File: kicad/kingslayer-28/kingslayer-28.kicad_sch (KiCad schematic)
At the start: 77 parts, among them IC1 STM32F303CCT7, IC3 LM3940IMP-3.3_NOPB, J1 Conn_01x04_Pin, K1 KEYSW, K10 KEYSW, K11 KEYSW, K12 KEYSW, K13 KEYSW, K14 KEYSW, K15 KEYSW, K16 KEYSW, K17 KEYSW, K18 KEYSW, K19 KEYSW, K2 KEYSW, K20 KEYSW, K21 KEYSW, K22 KEYSW, K23 KEYSW, K24 KEYSW, K25 KEYSW, K26 KEYSW, K27 KEYSW, K28 KEYSW, K3 KEYSW, K4 KEYSW, K5 KEYSW, K6 KEYSW, K7 KEYSW, K8 KEYSW, K9 KEYSW, SW1 MSS13PLP, X1 IC21008.000M30.0EE1B

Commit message: assign some footprints
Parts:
- D1, D10, D11, D12, D13, D14, D15, D16, D17, D18, D19, D2, D20, D21, D22, D23, D24, D25, D26, D27, D28, D3, D4, D5, D6, D7, D8, D9: footprint (none) -> 1N4148W_RHG:1N4148WRHG
- IC1: footprint QFP50P900X900X160-48N -> STM32F303CCT7:QFP50P900X900X160-48N
- IC3: footprint SOT230P700X180-4N -> LM3940IMP-3.3_NOPB:SOT230P700X180-4N
- K1, K10, K11, K12, K13, K14, K15, K16, K17, K18, K19, K2, K20, K21, K22, K23, K24, K25, K26, K27, K28, K3, K4, K5, K6, K7, K8, K9: footprint (none) -> keyswitches:Kailh_socket_MX
- S1: footprint TL3342F260QG -> TL3342F260QG:TL3342F260QG
- USB1: footprint (none) -> Type-C:USB_C_GCT_USB4085

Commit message: update mounting holes
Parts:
- added H1: MountingHole, keyswitches:Stabilizer_MX_2u, symbol Mechanical:MountingHole
- added H2, H3, H4, H5: MountingHole, MountingHole:MountingHole_2.2mm_M2_ISO7380, symbol Mechanical:MountingHole
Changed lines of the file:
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@@
+    )
+  )
+  (symbol (lib_id "Mechanical:MountingHole") (at 193.04 102.87 0) (unit 1)
+    (in_bom yes) (on_board yes) (dnp no) (fields_autoplaced)
+    (property "Reference" "H2" (at 195.58 101.6 0)
+      (effects (font (size 1.27 1.27)) (justify left))
+    )
+    (property "Value" "MountingHole" (at 195.58 104.14 0)
+      (effects (font (size 1.27 1.27)) (justify left))
+    )
+    (property "Footprint" "MountingHole:MountingHole_2.2mm_M2_ISO7380" (at 193.04 102.87 0)
+      (effects (font (size 1.27 1.27)) hide)
+    )
+    (property "Datasheet" "~" (at 193.04 102.87 0)
+      (effects (font (size 1.27 1.27)) hide)
+    )
+    (instances
+      (project "kingslayer-28"
+        (path "/7c3679ab-fb1a-4578-bd30-c0b9ef7b8f3d"
+          (reference "H2") (unit 1)
+        )
+      )
     )
   )
@@
     )
   )
+  (symbol (lib_id "Mechanical:MountingHole") (at 215.9 114.3 0) (unit 1)
+    (in_bom yes) (on_board yes) (dnp no) (fields_autoplaced)
+    (property "Reference" "H5" (at 218.44 113.03 0)
+      (effects (font (size 1.27 1.27)) (justify left))
+    )
+    (property "Value" "MountingHole" (at 218.44 115.57 0)
+      (effects (font (size 1.27 1.27)) (justify left))
+    )
+    (property "Footprint" "MountingHole:MountingHole_2.2mm_M2_ISO7380" (at 215.9 114.3 0)
+      (effects (font (size 1.27 1.27)) hide)
+    )
+    (property "Datasheet" "~" (at 215.9 114.3 0)
+      (effects (font (size 1.27 1.27)) hide)
+    )
+    (instances
+      (project "kingslayer-28"
+        (path "/7c3679ab-fb1a-4578-bd30-c0b9ef7b8f3d"
+          (reference "H5") (unit 1)
+        )
+      )
+    )
+  )
   (symbol (lib_id "keyboard_parts:+3V3") (at 237.49 38.1 0) (unit 1)
     (in_bom yes) (on_board yes) (dnp no) (fields_autoplaced)
@@
     )
   )
+  (symbol (lib_id "Mechanical:MountingHole") (at 137.16 81.28 0) (unit 1)
+    (in_bom yes) (on_board yes) (dnp no) (fields_autoplaced)
+    (property "Reference" "H1" (at 139.7 80.01 0)
+      (effects (font (size 1.27 1.27)) (justify left))
+    )
+    (property "Value" "MountingHole" (at 139.7 82.55 0)
+      (effects (font (size 1.27 1.27)) (justify left))
+    )
+    (property "Footprint" "keyswitches:Stabilizer_MX_2u" (at 137.16 81.28 0)
+      (effects (font (size 1.27 1.27)) hide)
+    )
+    (property "Datasheet" "~" (at 137.16 81.28 0)
+      (effects (font (size 1.27 1.27)) hide)
+    )
+    (instances
+      (project "kingslayer-28"
+        (path "/7c3679ab-fb1a-4578-bd30-c0b9ef7b8f3d"
+          (reference "H1") (unit 1)
+        )
+      )
+    )
+  )
   (symbol (lib_id "keyboard_parts:KEYSW") (at 71.12 39.37 0) (unit 1)
     (in_bom yes) (on_board yes) (dnp no)
@@
     )
   )
+  (symbol (lib_id "Mechanical:MountingHole") (at 193.04 114.3 0) (unit 1)
+    (in_bom yes) (on_board yes) (dnp no) (fields_autoplaced)
+    (property "Reference" "H4" (at 195.58 113.03 0)
+      (effects (font (size 1.27 1.27)) (justify left))
+    )
+    (property "Value" "MountingHole" (at 195.58 115.57 0)
+      (effects (font (size 1.27 1.27)) (justify left))
+    )
+    (property "Footprint" "MountingHole:MountingHole_2.2mm_M2_ISO7380" (at 193.04 114.3 0)
+      (effects (font (size 1.27 1.27)) hide)
+    )
+    (property "Datasheet" "~" (at 193.04 114.3 0)
+      (effects (font (size 1.27 1.27)) hide)
+    )
+    (instances
+      (project "kingslayer-28"
+        (path "/7c3679ab-fb1a-4578-bd30-c0b9ef7b8f3d"
+          (reference "H4") (unit 1)
+        )
+      )
+    )
+  )
   (symbol (lib_id "keyboard_parts:D") (at 63.5 82.55 180) (unit 1)
     (in_bom yes) (on_board yes) (dnp no) (fields_autoplaced)
@@
         )
       )
+    )
+  )
+  (symbol (lib_id "Mechanical:MountingHole") (at 215.9 102.87 0) (unit 1)
+    (in_bom yes) (on_board yes) (dnp no) (fields_autoplaced)
+    (property "Reference" "H3" (at 218.44 101.6 0)
+      (effects (font (size 1.27 1.27)) (justify left))
+    )
+    (property "Value" "MountingHole" (at 218.44 104.14 0)
+      (effects (font (size 1.27 1.27)) (justify left))
+    )
+    (property "Footprint" "MountingHole:MountingHole_2.2mm_M2_ISO7380" (at 215.9 102.87 0)
+      (effects (font (size 1.27 1.27)) hide)
+    )
+    (property "Datasheet" "~" (at 215.9 102.87 0)
+      (effects (font (size 1.27 1.27)) hide)
+    )
+    (instances
+      (project "kingslayer-28"
+        (path "/7c3679ab-fb1a-4578-bd30-c0b9ef7b8f3d"
+          (reference "H3") (unit 1)
+        )
+      )

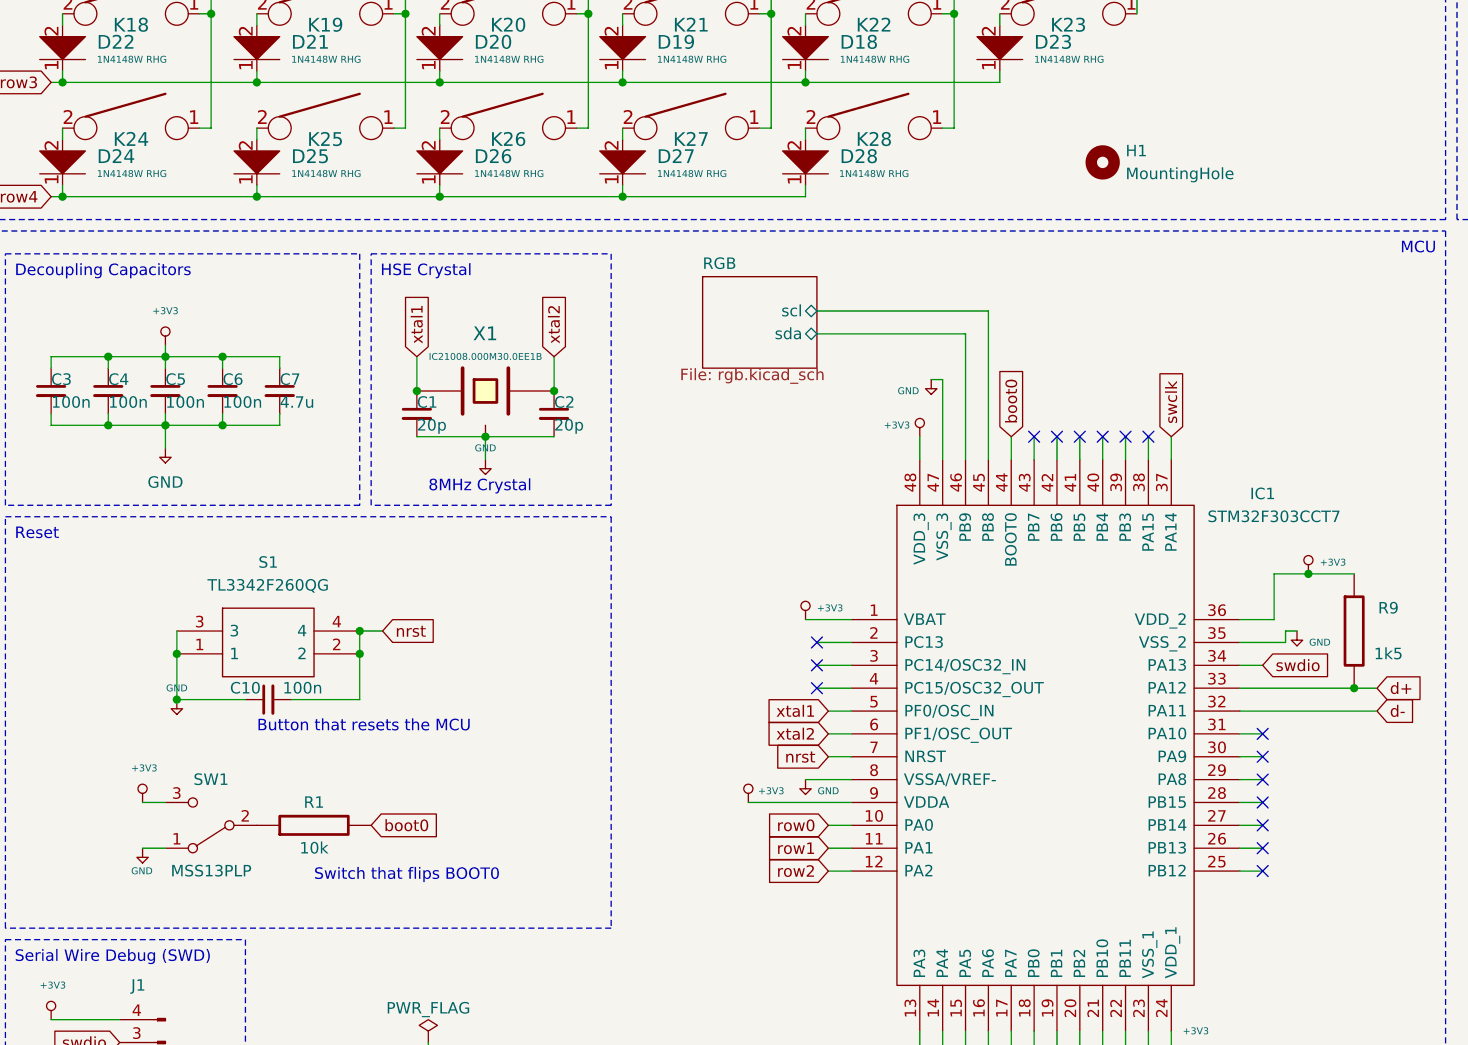
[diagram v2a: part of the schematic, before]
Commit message: header, switch, oscillator
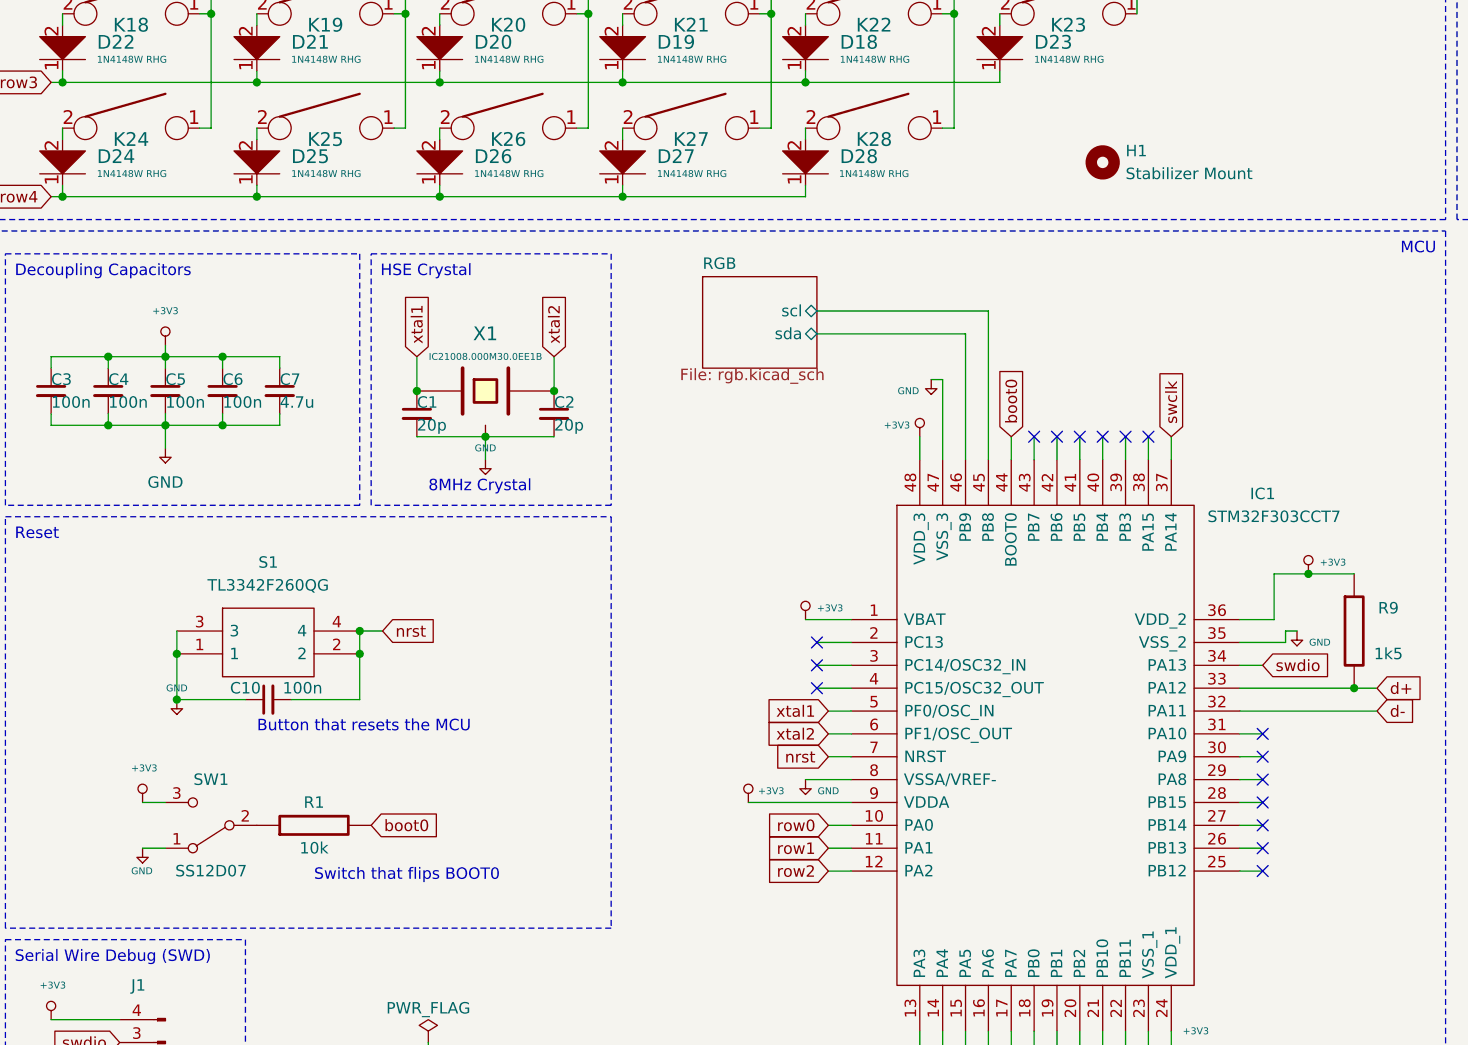
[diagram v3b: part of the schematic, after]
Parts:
- H1: value MountingHole -> Stabilizer Mount
- J1: footprint (none) -> Connector_PinHeader_2.00mm:PinHeader_1x04_P2.00mm_Vertical
- SW1: value MSS13PLP -> SS12D07; footprint (none) -> SS12D07VG4:SW_SS12D07VG4
- X1: footprint (none) -> Crystal:Crystal_SMD_HC49-SD_HandSoldering
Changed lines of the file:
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@@
       (effects (font (size 1.27 1.27)))
     )
-    (property "Value" "MSS13PLP" (at 38.1 160.02 0)
+    (property "Value" "SS12D07" (at 38.1 160.02 0)
       (effects (font (size 1.27 1.27)))
     )
-    (property "Footprint" "" (at 38.1 154.94 0)
+    (property "Footprint" "SS12D07VG4:SW_SS12D07VG4" (at 38.1 154.94 0)
       (effects (font (size 1.27 1.27)) hide)
     )
@@
       (effects (font (size 0.762 0.762)))
     )
-    (property "Footprint" "" (at 68.58 106.68 0)
+    (property "Footprint" "Crystal:Crystal_SMD_HC49-SD_HandSoldering" (at 68.58 106.68 0)
       (effects (font (size 1.524 1.524)) hide)
     )
@@
       (effects (font (size 1.27 1.27)) (justify right))
     )
-    (property "Footprint" "" (at 33.02 181.61 0)
+    (property "Footprint" "Connector_PinHeader_2.00mm:PinHeader_1x04_P2.00mm_Vertical" (at 33.02 181.61 0)
       (effects (font (size 1.27 1.27)) hide)
     )
@@
       (effects (font (size 1.27 1.27)) (justify left))
     )
-    (property "Value" "MountingHole" (at 139.7 82.55 0)
-      (effects (font (size 1.27 1.27)) (justify left))
-    )
+    (property "Value" "Stabilizer Mount" (at 139.7 82.55 0)
+      (effects (font (size 1.27 1.27)) (justify left))
+    )

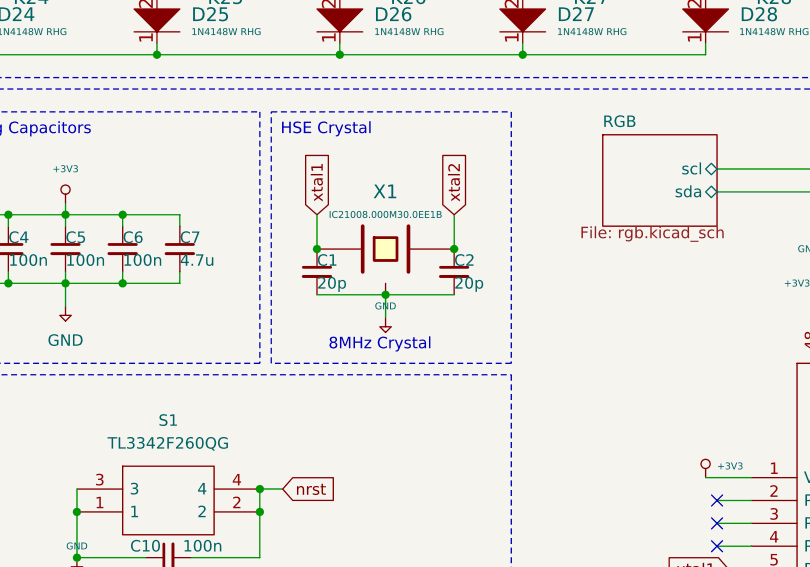
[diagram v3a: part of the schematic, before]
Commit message: footprint mapping
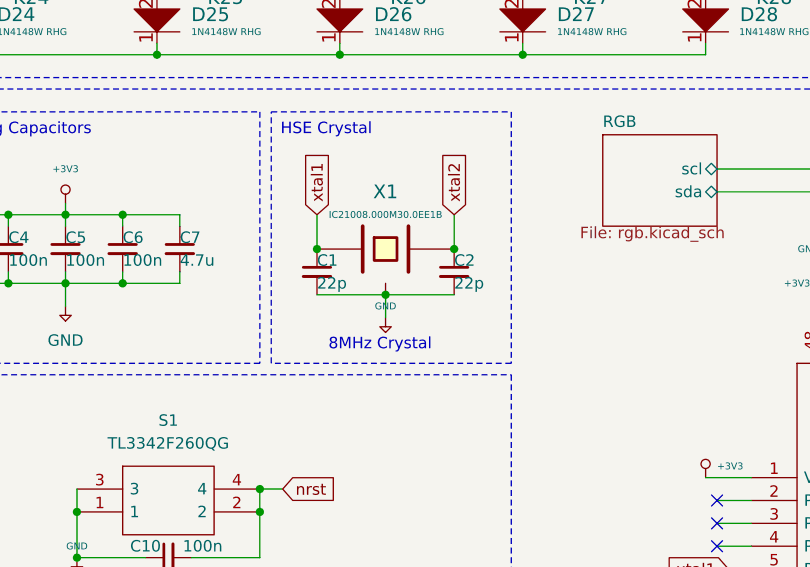
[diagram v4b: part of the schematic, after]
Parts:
- C1, C2: value 20p -> 22p; footprint (none) -> Capacitor_SMD:C_0603_1608Metric_Pad1.08x0.95mm_HandSolder
- C10, C3, C4, C5, C6: footprint (none) -> 08053C104KAT2A:CAPC2012X94N
- C11, C7: footprint (none) -> Capacitor_SMD:C_0805_2012Metric_Pad1.18x1.45mm_HandSolder
- C12: footprint (none) -> Capacitor_Tantalum_SMD:CP_EIA-7343-31_Kemet-D_Pad2.25x2.55mm_HandSolder
- R1: footprint (none) -> RMCF0805JT10K0:RESC2012X65N
- R7, R8: footprint (none) -> CR0805-FX-5101ELF:RESC2012X60N
- R9: footprint (none) -> Resistor_SMD:R_1206_3216Metric_Pad1.30x1.75mm_HandSolder
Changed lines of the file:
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@@
       (effects (font (size 1.27 1.27)))
     )
-    (property "Footprint" "" (at 49.53 154.94 0)
+    (property "Footprint" "RMCF0805JT10K0:RESC2012X65N" (at 49.53 154.94 0)
       (effects (font (size 1.524 1.524)) hide)
     )
@@
       (effects (font (size 1.27 1.27)))
     )
-    (property "Footprint" "" (at 224.79 29.21 0)
+    (property "Footprint" "CR0805-FX-5101ELF:RESC2012X60N" (at 224.79 29.21 0)
       (effects (font (size 1.524 1.524)) hide)
     )
@@
       (effects (font (size 1.27 1.27)))
     )
-    (property "Footprint" "" (at 165.1 133.35 0)
+    (property "Footprint" "Resistor_SMD:R_1206_3216Metric_Pad1.30x1.75mm_HandSolder" (at 165.1 133.35 0)
       (effects (font (size 1.524 1.524)) hide)
     )
@@
       (effects (font (size 1.27 1.27)) (justify left))
     )
-    (property "Value" "20p" (at 60.96 110.49 0)
-      (effects (font (size 1.27 1.27)) (justify left))
-    )
-    (property "Footprint" "" (at 60.96 109.22 0)
+    (property "Value" "22p" (at 60.96 110.49 0)
+      (effects (font (size 1.27 1.27)) (justify left))
+    )
+    (property "Footprint" "Capacitor_SMD:C_0603_1608Metric_Pad1.08x0.95mm_HandSolder" (at 60.96 109.22 0)
       (effects (font (size 1.27 1.27)) hide)
     )
@@
       (effects (font (size 1.27 1.27)) (justify left))
     )
-    (property "Footprint" "" (at 33.02 106.68 0)
+    (property "Footprint" "08053C104KAT2A:CAPC2012X94N" (at 33.02 106.68 0)
       (effects (font (size 1.27 1.27)) hide)
     )
@@
       (effects (font (size 1.27 1.27)) (justify left))
     )
-    (property "Footprint" "" (at 45.72 106.68 0)
+    (property "Footprint" "Capacitor_SMD:C_0805_2012Metric_Pad1.18x1.45mm_HandSolder" (at 45.72 106.68 0)
       (effects (font (size 1.27 1.27)) hide)
     )
@@
       (effects (font (size 1.27 1.27)))
     )
-    (property "Footprint" "" (at 224.79 31.75 0)
+    (property "Footprint" "CR0805-FX-5101ELF:RESC2012X60N" (at 224.79 31.75 0)
       (effects (font (size 1.524 1.524)) hide)
     )
@@
       (effects (font (size 1.27 1.27)) (justify left))
     )
-    (property "Footprint" "" (at 20.32 106.68 0)
+    (property "Footprint" "08053C104KAT2A:CAPC2012X94N" (at 20.32 106.68 0)
       (effects (font (size 1.27 1.27)) hide)
     )
@@
       (effects (font (size 1.27 1.27)) (justify left))
     )
-    (property "Value" "20p" (at 76.2 110.49 0)
-      (effects (font (size 1.27 1.27)) (justify left))
-    )
-    (property "Footprint" "" (at 76.2 109.22 0)
+    (property "Value" "22p" (at 76.2 110.49 0)
+      (effects (font (size 1.27 1.27)) (justify left))
+    )
+    (property "Footprint" "Capacitor_SMD:C_0603_1608Metric_Pad1.08x0.95mm_HandSolder" (at 76.2 109.22 0)
       (effects (font (size 1.27 1.27)) hide)
     )
@@
       (effects (font (size 1.27 1.27)) (justify left))
     )
-    (property "Footprint" "" (at 237.49 48.26 0)
+    (property "Footprint" "Capacitor_Tantalum_SMD:CP_EIA-7343-31_Kemet-D_Pad2.25x2.55mm_HandSolder" (at 237.49 48.26 0)
       (effects (font (size 1.27 1.27)) hide)
     )
@@
       (effects (font (size 1.27 1.27)) (justify left))
     )
-    (property "Footprint" "" (at 26.67 106.68 0)
+    (property "Footprint" "08053C104KAT2A:CAPC2012X94N" (at 26.67 106.68 0)
       (effects (font (size 1.27 1.27)) hide)
     )
@@
       (effects (font (size 1.27 1.27)) (justify left))
     )
-    (property "Footprint" "" (at 39.37 106.68 0)
+    (property "Footprint" "08053C104KAT2A:CAPC2012X94N" (at 39.37 106.68 0)
       (effects (font (size 1.27 1.27)) hide)
     )
@@
       (effects (font (size 1.27 1.27)) (justify left))
     )
-    (property "Footprint" "" (at 226.06 48.26 0)
+    (property "Footprint" "Capacitor_SMD:C_0805_2012Metric_Pad1.18x1.45mm_HandSolder" (at 226.06 48.26 0)
       (effects (font (size 1.27 1.27)) hide)
     )
@@
       (effects (font (size 1.27 1.27)))
     )
-    (property "Footprint" "" (at 44.45 140.97 0)
-      (effects (font (size 1.27 1.27)) hide)
-    )
+    (property "Footprint" "08053C104KAT2A:CAPC2012X94N" (at 44.45 140.97 0)
+      (effects (font (size 1.27 1.27)) hide)
+    )

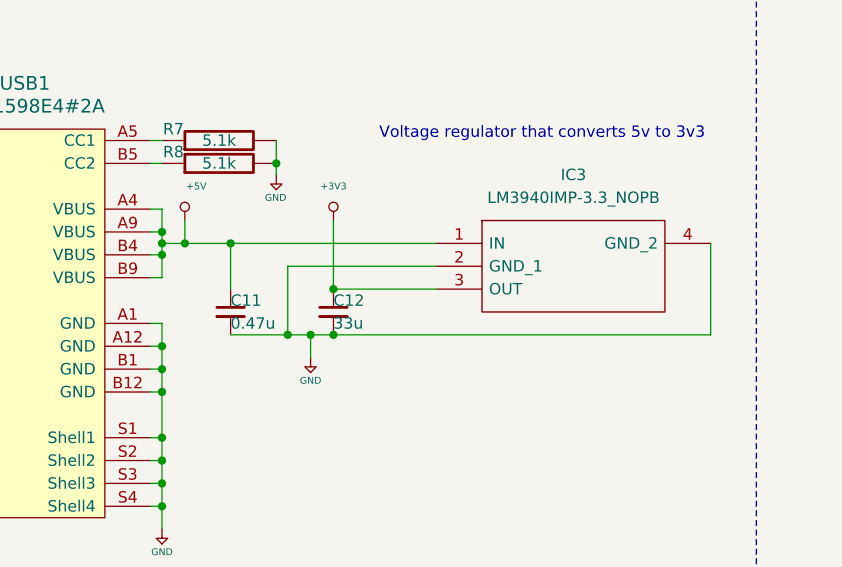
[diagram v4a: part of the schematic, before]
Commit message: Add fuse because of tantalum cap
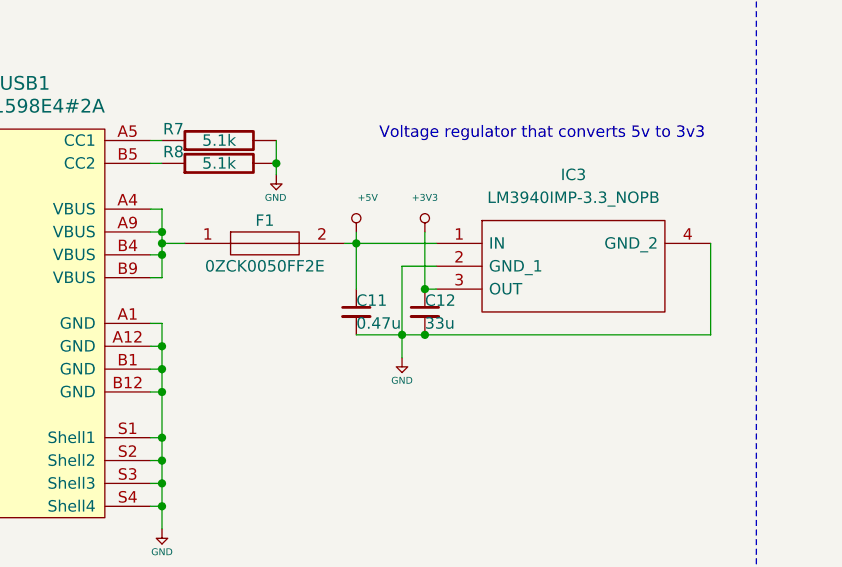
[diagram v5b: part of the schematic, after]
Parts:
- added F1: 0ZCK0050FF2E, 0ZCK0050FF2E:FUSC2214X125N, symbol 0ZCK0050FF2E:0ZCK0050FF2E
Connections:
- net +5V: now also F1.2; no longer USB1.A4 (VBUS), USB1.A9 (VBUS), USB1.B4 (VBUS), USB1.B9 (VBUS)
- new net: F1.1, USB1.A4 (VBUS), USB1.A9 (VBUS), USB1.B4 (VBUS), USB1.B9 (VBUS)
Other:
- moved on the sheet: C11, C12
